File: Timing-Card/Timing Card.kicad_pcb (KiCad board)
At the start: 4 copper layers, 65 x 41.6 mm, 140 parts, among them J1 71430-0101, J10 10018784-10201TLF, J2 Conn_01x10, U1 LCMXO2-7000HC-6TG144I, U10 74AHC125, U11 T602-025.0M, U12 FM24C64B, U2 SN74LVC1G125DRL, U3 74AHCT125, U4 74AHCT125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

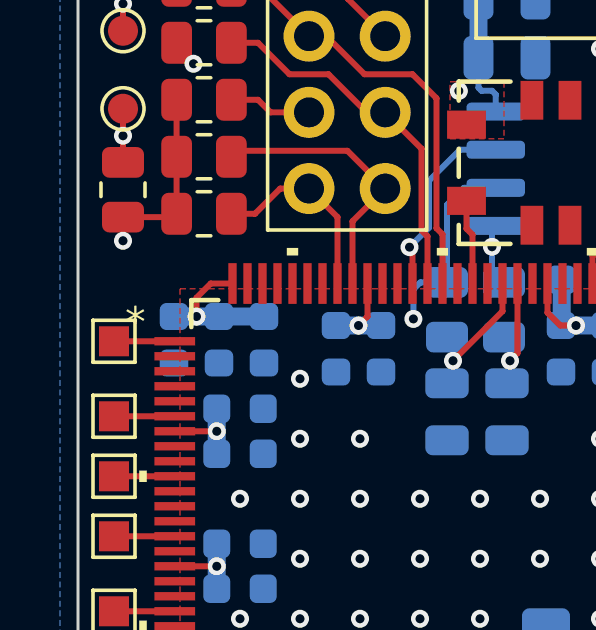
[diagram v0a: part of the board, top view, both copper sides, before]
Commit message: Camera Control Card layout
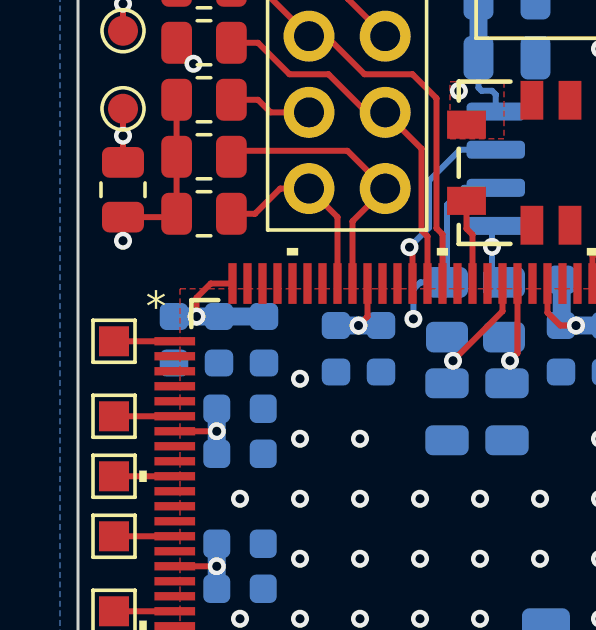
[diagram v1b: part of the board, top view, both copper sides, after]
